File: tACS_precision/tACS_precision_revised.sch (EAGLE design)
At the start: 48 parts, among them IC1 TLC2252, IC2 LM4040, IC3 TLC2252, IC4 LM4040, IC5 ADR5041, IC6 REF5050AIDR, IC7 L78L05, T1 FMMT734, T2 FMMT634, T3 FMMT634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

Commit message: patched board layout
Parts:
- removed IC5: ADR5041, texas:LM4041D12DBZ
- added U$3: ADR5041, precision_tACS:ADR5041BKSZ
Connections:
- net N$15: now also U$3.ANODE; no longer IC5.A
- net N$16: now also U$3.CATHODE; no longer IC5.C
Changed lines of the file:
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@@
 <part name="R11" library="rcl" deviceset="R-US_" device="R0603" value="7K15"/>
 <part name="T6" library="zetex" deviceset="FMMT6*" device="" technology="24" value="FMMT634"/>
-<part name="IC5" library="texas" deviceset="LM4041" device="DBZ" technology="D12" value="ADR5041"/>
 <part name="C1" library="rcl" deviceset="C-EU" device="C1608" value="1uF"/>
 <part name="R12" library="rcl" deviceset="R-US_" device="R2512" value="2K2"/>
@@
 <part name="H1" library="holes" deviceset="MOUNT-HOLE" device="5.5"/>
 <part name="H2" library="holes" deviceset="MOUNT-HOLE" device="5.5"/>
+<part name="U$3" library="precision_tACS" deviceset="ADR5041BKSZ" device="" value="ADR5041"/>
 </parts>
 <sheets>
@@
 <instance part="IC1" gate="P" x="106.68" y="78.74"/>
 <instance part="IC3" gate="P" x="106.68" y="12.7"/>
-<instance part="IC5" gate="G$1" x="86.36" y="60.96"/>
 <instance part="C1" gate="G$1" x="71.12" y="-15.24"/>
 <instance part="R12" gate="G$1" x="152.4" y="45.72"/>
@@
 <instance part="H1" gate="G$1" x="-10.16" y="-15.24"/>
 <instance part="H2" gate="G$1" x="-10.16" y="-22.86"/>
+<instance part="U$3" gate="G$1" x="86.36" y="53.34"/>
 </instances>
 <busses>
@@
 <pinref part="IC1" gate="A" pin="+IN"/>
 <wire x1="96.52" y1="81.28" x2="99.06" y2="81.28" width="0.1524" layer="91"/>
+<pinref part="U$3" gate="G$1" pin="ANODE"/>
 <junction x="86.36" y="53.34"/>
-<pinref part="IC5" gate="G$1" pin="A"/>
-<wire x1="86.36" y1="58.42" x2="86.36" y2="53.34" width="0.1524" layer="91"/>
 </segment>
 </net>
@@
 <wire x1="99.06" y1="68.58" x2="86.36" y2="68.58" width="0.1524" layer="91"/>
 <junction x="99.06" y="68.58"/>
-<junction x="86.36" y="68.58"/>
 <pinref part="IC1" gate="P" pin="V-"/>
 <wire x1="106.68" y1="71.12" x2="106.68" y2="68.58" width="0.1524" layer="91"/>
 <junction x="106.68" y="68.58"/>
-<pinref part="IC5" gate="G$1" pin="C"/>
-<wire x1="86.36" y1="63.5" x2="86.36" y2="68.58" width="0.1524" layer="91"/>
-</segment>
-</net>
+<pinref part="U$3" gate="G$1" pin="CATHODE"/>
+<junction x="86.36" y="68.58"/>
+</segment>
+</net>

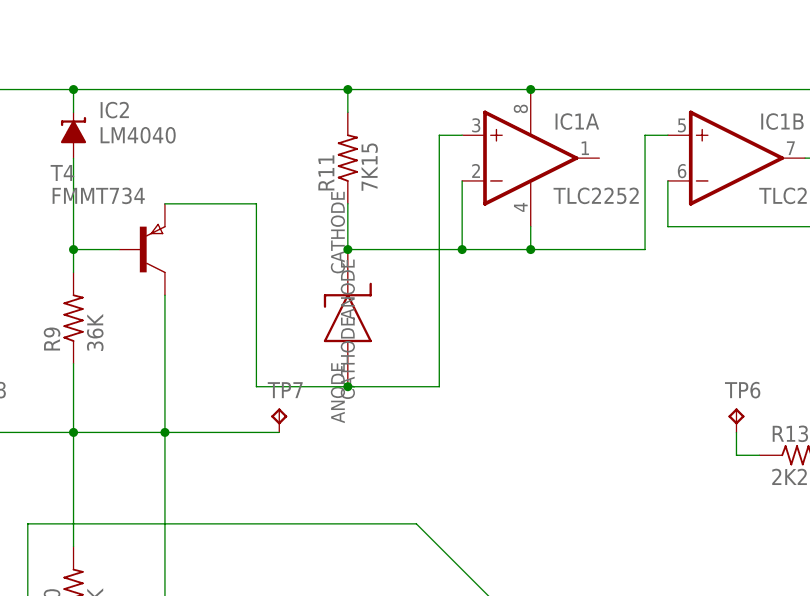
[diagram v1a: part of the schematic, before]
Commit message: Board fixed, firmware written, all tested
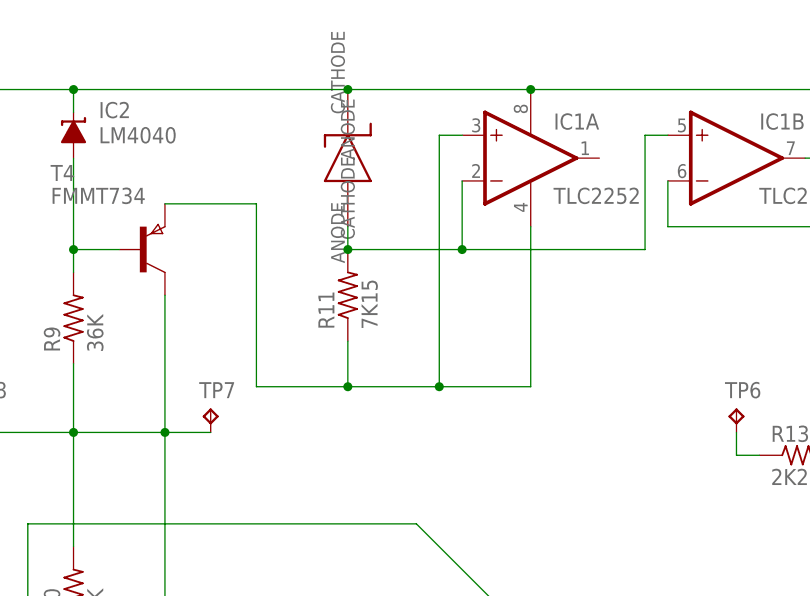
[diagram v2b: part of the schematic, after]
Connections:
- net N$15: now also IC1P.V-, R11.1; no longer U$3.ANODE
- net N$16: now also R11.2, U$3.ANODE; no longer IC1P.V-, R11.1, U$3.CATHODE
- net N$8: now also U$3.CATHODE; no longer R11.2
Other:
- moved on the sheet: R11, TP7
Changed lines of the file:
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@@
 <instance part="T4" gate="G$1" x="63.5" y="68.58"/>
 <instance part="T5" gate="G$1" x="162.56" y="63.5"/>
-<instance part="R11" gate="G$1" x="86.36" y="78.74" rot="R90"/>
+<instance part="R11" gate="G$1" x="86.36" y="63.5" rot="R90"/>
 <instance part="T6" gate="G$1" x="162.56" y="12.7"/>
 <instance part="IC1" gate="P" x="106.68" y="78.74"/>
@@
 <instance part="C3" gate="G$1" x="58.42" y="-15.24"/>
 <instance part="TP6" gate="G$1" x="129.54" y="50.8"/>
-<instance part="TP7" gate="G$1" x="78.74" y="50.8"/>
+<instance part="TP7" gate="G$1" x="71.12" y="50.8"/>
 <instance part="TP8" gate="G$1" x="45.72" y="50.8"/>
 <instance part="TP9" gate="G$1" x="-5.08" y="88.9"/>
@@
 <instance part="H1" gate="G$1" x="-10.16" y="-15.24"/>
 <instance part="H2" gate="G$1" x="-10.16" y="-22.86"/>
-<instance part="U$3" gate="G$1" x="86.36" y="53.34"/>
+<instance part="U$3" gate="G$1" x="86.36" y="71.12"/>
 </instances>
 <busses>
@@
 <wire x1="165.1" y1="83.82" x2="165.1" y2="86.36" width="0.1524" layer="91"/>
 <wire x1="165.1" y1="86.36" x2="106.68" y2="86.36" width="0.1524" layer="91"/>
-<pinref part="R11" gate="G$1" pin="2"/>
 <wire x1="106.68" y1="86.36" x2="86.36" y2="86.36" width="0.1524" layer="91"/>
-<wire x1="86.36" y1="86.36" x2="55.88" y2="86.36" width="0.1524" layer="91"/>
-<wire x1="86.36" y1="83.82" x2="86.36" y2="86.36" width="0.1524" layer="91"/>
-<junction x="86.36" y="86.36"/>
 <pinref part="IC1" gate="P" pin="V+"/>
 <junction x="106.68" y="86.36"/>
+<pinref part="U$3" gate="G$1" pin="CATHODE"/>
+<wire x1="86.36" y1="86.36" x2="55.88" y2="86.36" width="0.1524" layer="91"/>
+<junction x="86.36" y="86.36"/>
 </segment>
 </net>
@@
 <wire x1="45.72" y1="48.26" x2="55.88" y2="48.26" width="0.1524" layer="91"/>
 <pinref part="TP7" gate="G$1" pin="TP"/>
-<wire x1="78.74" y1="48.26" x2="66.04" y2="48.26" width="0.1524" layer="91"/>
+<wire x1="71.12" y1="48.26" x2="66.04" y2="48.26" width="0.1524" layer="91"/>
 </segment>
 </net>
@@
 </segment>
 </net>
-<net name="N$15" class="0">
-<segment>
-<pinref part="T4" gate="G$1" pin="E"/>
-<wire x1="66.04" y1="73.66" x2="76.2" y2="73.66" width="0.1524" layer="91"/>
-<wire x1="76.2" y1="73.66" x2="76.2" y2="53.34" width="0.1524" layer="91"/>
-<wire x1="76.2" y1="53.34" x2="86.36" y2="53.34" width="0.1524" layer="91"/>
-<wire x1="86.36" y1="53.34" x2="96.52" y2="53.34" width="0.1524" layer="91"/>
-<wire x1="96.52" y1="53.34" x2="96.52" y2="81.28" width="0.1524" layer="91"/>
-<pinref part="IC1" gate="A" pin="+IN"/>
-<wire x1="96.52" y1="81.28" x2="99.06" y2="81.28" width="0.1524" layer="91"/>
-<pinref part="U$3" gate="G$1" pin="ANODE"/>
-<junction x="86.36" y="53.34"/>
-</segment>
-</net>
 <net name="N$16" class="0">
 <segment>
@@
 <wire x1="121.92" y1="81.28" x2="119.38" y2="81.28" width="0.1524" layer="91"/>
 <wire x1="119.38" y1="81.28" x2="119.38" y2="68.58" width="0.1524" layer="91"/>
-<wire x1="119.38" y1="68.58" x2="106.68" y2="68.58" width="0.1524" layer="91"/>
+<wire x1="119.38" y1="68.58" x2="99.06" y2="68.58" width="0.1524" layer="91"/>
 <pinref part="IC1" gate="A" pin="-IN"/>
-<wire x1="106.68" y1="68.58" x2="99.06" y2="68.58" width="0.1524" layer="91"/>
 <wire x1="99.06" y1="68.58" x2="99.06" y2="76.2" width="0.1524" layer="91"/>
-<pinref part="R11" gate="G$1" pin="1"/>
-<wire x1="86.36" y1="73.66" x2="86.36" y2="68.58" width="0.1524" layer="91"/>
+<pinref part="R11" gate="G$1" pin="2"/>
 <wire x1="99.06" y1="68.58" x2="86.36" y2="68.58" width="0.1524" layer="91"/>
 <junction x="99.06" y="68.58"/>
-<pinref part="IC1" gate="P" pin="V-"/>
-<wire x1="106.68" y1="71.12" x2="106.68" y2="68.58" width="0.1524" layer="91"/>
-<junction x="106.68" y="68.58"/>
-<pinref part="U$3" gate="G$1" pin="CATHODE"/>
+<pinref part="U$3" gate="G$1" pin="ANODE"/>
+<wire x1="86.36" y1="68.58" x2="86.36" y2="71.12" width="0.1524" layer="91"/>
 <junction x="86.36" y="68.58"/>
 </segment>
@@
 </segment>
 </net>
+<net name="N$15" class="0">
+<segment>
+<pinref part="T4" gate="G$1" pin="E"/>
+<wire x1="66.04" y1="73.66" x2="76.2" y2="73.66" width="0.1524" layer="91"/>
+<wire x1="76.2" y1="73.66" x2="76.2" y2="53.34" width="0.1524" layer="91"/>
+<wire x1="96.52" y1="53.34" x2="96.52" y2="81.28" width="0.1524" layer="91"/>
+<pinref part="IC1" gate="A" pin="+IN"/>
+<wire x1="96.52" y1="81.28" x2="99.06" y2="81.28" width="0.1524" layer="91"/>
+<pinref part="IC1" gate="P" pin="V-"/>
+<wire x1="96.52" y1="53.34" x2="106.68" y2="53.34" width="0.1524" layer="91"/>
+<wire x1="106.68" y1="53.34" x2="106.68" y2="71.12" width="0.1524" layer="91"/>
+<wire x1="76.2" y1="53.34" x2="86.36" y2="53.34" width="0.1524" layer="91"/>
+<junction x="96.52" y="53.34"/>
+<pinref part="R11" gate="G$1" pin="1"/>
+<wire x1="86.36" y1="53.34" x2="96.52" y2="53.34" width="0.1524" layer="91"/>
+<wire x1="86.36" y1="58.42" x2="86.36" y2="53.34" width="0.1524" layer="91"/>
+<junction x="86.36" y="53.34"/>
+</segment>
+</net>
